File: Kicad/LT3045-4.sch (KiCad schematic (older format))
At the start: 22 parts, among them J1 Conn_Coaxial_Power, J2 Conn_Coaxial_Power, U1 LT3042, U2 LT3042, U3 LT3042, U4 LT3042

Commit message: 1st design
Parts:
- C3, C7, C8, C9: symbol Device:C_SPLIT -> LT3045-4-rescue:C_SPLIT-Device-LNA-rescue
- U1, U2, U3, U4: symbol Regulator_Linear:LT3042 -> LT3045-4-rescue:LT3042-Regulator_Linear-LNA-rescue
- gave numbers to parts that had none: 1
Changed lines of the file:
@@
 $EndComp
 $Comp
-L Regulator_Linear:LT3042 U1
+L LT3045-4-rescue:LT3042-Regulator_Linear-LNA-rescue U1
 U 1 1 5F2966C9
 P 5000 1150
@@
 	2700 900  2950 900
 $Comp
-L Device:C_SPLIT C3
+L LT3045-4-rescue:C_SPLIT-Device-LNA-rescue C3
 U 1 1 5F3E0394
 P 5850 1350
@@
 $EndComp
 $Comp
-L Regulator_Linear:LT3042 U2
+L LT3045-4-rescue:LT3042-Regulator_Linear-LNA-rescue U2
 U 1 1 5F43CBE8
 P 5000 3000
@@
 50mOhm\nTrace
 $Comp
-L Device:C_SPLIT C7
+L LT3045-4-rescue:C_SPLIT-Device-LNA-rescue C7
 U 1 1 5F43CC30
 P 5850 3200
@@
 $EndComp
 $Comp
-L Regulator_Linear:LT3042 U3
+L LT3045-4-rescue:LT3042-Regulator_Linear-LNA-rescue U3
 U 1 1 5F442849
 P 5000 4750
@@
 50mOhm\nTrace
 $Comp
-L Device:C_SPLIT C8
+L LT3045-4-rescue:C_SPLIT-Device-LNA-rescue C8
 U 1 1 5F442891
 P 5850 4950
@@
 $EndComp
 $Comp
-L Regulator_Linear:LT3042 U4
+L LT3045-4-rescue:LT3042-Regulator_Linear-LNA-rescue U4
 U 1 1 5F44B383
 P 5000 6600
@@
 50mOhm\nTrace
 $Comp
-L Device:C_SPLIT C9
+L LT3045-4-rescue:C_SPLIT-Device-LNA-rescue C9
 U 1 1 5F44B3CB
 P 5850 6800
@@
 VIN
 $Comp
-L Device:R_US R?
+L Device:R_US R1
 U 1 1 5FCF17CA
 P 4250 1250
-F 0 "R?" H 4318 1296 50  0000 L CNN
+F 0 "R1" H 4318 1296 50  0000 L CNN
 F 1 "200k" H 4318 1205 50  0000 L CNN
 F 2 "Resistor_SMD:R_0603_1608Metric" V 4290 1240 50  0001 C CNN

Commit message: VIAS
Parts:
- added C11, C4, C5, C6: 4.7µF 35V, Capacitor_SMD:C_0805_2012Metric, symbol Device:C
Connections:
- net GND_SET1: now also C11.2, C4.2, C5.2, C6.2
- net at C2.1, R3.1, U1.7 (SET)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: now also C11.1, C4.1, C5.1, C6.1
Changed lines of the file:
@@
 	2300 1500 1700 1500
-Wire Wire Line
-	4200 1750 4000 1750
-Wire Wire Line
-	4000 1750 4000 3600
 Wire Wire Line
 	4000 3600 4750 3600
@@
 	4750 5250 4750 5350
 Wire Wire Line
-	4750 5350 4000 5350
-Wire Wire Line
-	4000 5350 4000 3600
-Connection ~ 4000 3600
-Wire Wire Line
 	4750 7100 4750 7200
-Wire Wire Line
-	4750 7200 4000 7200
-Wire Wire Line
-	4000 7200 4000 5350
-Connection ~ 4000 5350
 Connection ~ 4200 2200
 Wire Wire Line
@@
 Wire Wire Line
 	5750 3450 5750 4150
+$Comp
+L Device:C C4
+U 1 1 5FD57A1A
+P 3950 2000
+F 0 "C4" H 4065 2046 50  0000 L CNN
+F 1 "4.7µF 35V" H 4065 1955 50  0000 L CNN
+F 2 "Capacitor_SMD:C_0805_2012Metric" H 3988 1850 50  0001 C CNN
+F 3 "~" H 3950 2000 50  0001 C CNN
+	1    3950 2000
+	1    0    0    -1
+$EndComp
+$Comp
+L Device:C C5
+U 1 1 5FD5D837
+P 4000 3850
+F 0 "C5" H 4115 3896 50  0000 L CNN
+F 1 "4.7µF 35V" H 4115 3805 50  0000 L CNN
+F 2 "Capacitor_SMD:C_0805_2012Metric" H 4038 3700 50  0001 C CNN
+F 3 "~" H 4000 3850 50  0001 C CNN
+	1    4000 3850
+	1    0    0    -1
+$EndComp
+$Comp
+L Device:C C6
+U 1 1 5FD6373A
+P 4000 5600
+F 0 "C6" H 4115 5646 50  0000 L CNN
+F 1 "4.7µF 35V" H 4115 5555 50  0000 L CNN
+F 2 "Capacitor_SMD:C_0805_2012Metric" H 4038 5450 50  0001 C CNN
+F 3 "~" H 4000 5600 50  0001 C CNN
+	1    4000 5600
+	1    0    0    -1
+$EndComp
+$Comp
+L Device:C C11
+U 1 1 5FD69ACD
+P 4000 7450
+F 0 "C11" H 4115 7496 50  0000 L CNN
+F 1 "4.7µF 35V" H 4115 7405 50  0000 L CNN
+F 2 "Capacitor_SMD:C_0805_2012Metric" H 4038 7300 50  0001 C CNN
+F 3 "~" H 4000 7450 50  0001 C CNN
+	1    4000 7450
+	1    0    0    -1
+$EndComp
+Wire Wire Line
+	3950 1750 3950 1850
+Connection ~ 3950 1750
+Wire Wire Line
+	3950 1750 4200 1750
+Wire Wire Line
+	4000 3700 4000 3600
+Wire Wire Line
+	3750 1750 3750 3600
+Wire Wire Line
+	3750 3600 4000 3600
+Wire Wire Line
+	3750 1750 3950 1750
+Connection ~ 4000 3600
+Wire Wire Line
+	3750 3600 3750 5350
+Wire Wire Line
+	3750 5350 4000 5350
+Connection ~ 3750 3600
+Wire Wire Line
+	4000 5450 4000 5350
+Connection ~ 4000 5350
+Wire Wire Line
+	4000 5350 4750 5350
+Wire Wire Line
+	4200 5950 4000 5950
+Wire Wire Line
+	4000 5950 4000 5750
+Wire Wire Line
+	4200 4150 4000 4150
+Wire Wire Line
+	4000 4150 4000 4000
+Wire Wire Line
+	4200 2200 3950 2200
+Wire Wire Line
+	3950 2200 3950 2150
+Wire Wire Line
+	3750 5350 3750 7200
+Connection ~ 3750 5350
+Wire Wire Line
+	3750 7200 4000 7200
+Wire Wire Line
+	4000 7300 4000 7200
+Connection ~ 4000 7200
+Wire Wire Line
+	4000 7200 4750 7200
+Wire Wire Line
+	4000 7600 4000 7750
+Wire Wire Line
+	4000 7750 4200 7750
+Connection ~ 4200 7750
 $EndSCHEMATC

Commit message: Lost revision :(
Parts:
- added C12: 22µF 35V, Capacitor_Tantalum_SMD:CP_EIA-7343-30_AVX-N, symbol Device:CP1
- added C13: 4.7µF 35V, Capacitor_SMD:C_0805_2012Metric, symbol Device:C
- added F1: 4A, Fuse:Fuse_Bourns_MF-SM_9.5x6.71mm, symbol Device:Polyfuse_Small
- added L1: DLW5BTH101TQ2L, Transformer_SMD:CMC_DLW5BTH, symbol Device:Common_Mode_Choke
- added MH1, MH2, MH3, MH4: MountingHole_Pad, MountingHole:MountingHole_3.2mm_M3, symbol Mechanical:MountingHole_Pad
- added R2: 16.5k, Resistor_SMD:R_0603_1608Metric, symbol Device:R_US
- added Rcdc1: Rcdc, Resistor_SMD:R_0603_1608Metric, symbol Device:R_US
- RIlim1: renamed from R14; value 0 -> 287
- RIlim2: renamed from R4; value 0 -> 287
- RIlim3: renamed from R15; value 0 -> 287
- RIlim4: renamed from R16; value 0 -> 287
- renumbered L1 to L2, R3 to Rset1
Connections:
- net GND: now also C12.2, C13.2, L1.3, MH1.1, MH2.1, MH3.1, MH4.1, Rcdc1.2; no longer J1.2 (Ext), RIlim1.2, RIlim2.2, RIlim3.2, RIlim4.2
- net at C11.1, C2.1, C4.1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: now also R2.1
- net at C1.1, C10.1, L2.2: now also C12.1, C13.1, L1.2; no longer J1.1 (In)
- new net: F1.2, J1.1 (In)
- new net: J1.2 (Ext), L1.4
- new net: F1.1, L1.1
- new net ILim: R2.2, RIlim1.2, RIlim2.2, RIlim3.2, RIlim4.2, Rcdc1.1
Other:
- note added: "20/50mOhm\nTrace"
- note added: "Res = width length PCB weigth Temp \n50mOhm = 0.1mm 27.6mm 2oz/ft² -40C\n = 0.2mm 27.6mm 1oz/ft² -40C\n = 0.4mm 27.6mm 0.5oz/ft² -40C\n20mOhm = 0.25mm 27.6mm 2oz/ft² -40C\n = 0.5mm 27.6mm 1oz/ft² -40C\n = 1.0mm 27.6mm 0.5oz/ft² -40C"
- note removed: "50mOhm\nTrace"
- note removed: "Res = width length PCB weigth Temp \n50mOhm = 0.1mm 27.6mm 2oz/ft² -40C\n = 0.2mm 27.6mm 1oz/ft² -40C\n"
- moved on the sheet: C1, C10, C11, C2, C3, C4, C5, C6, C7, C8, C9, J1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

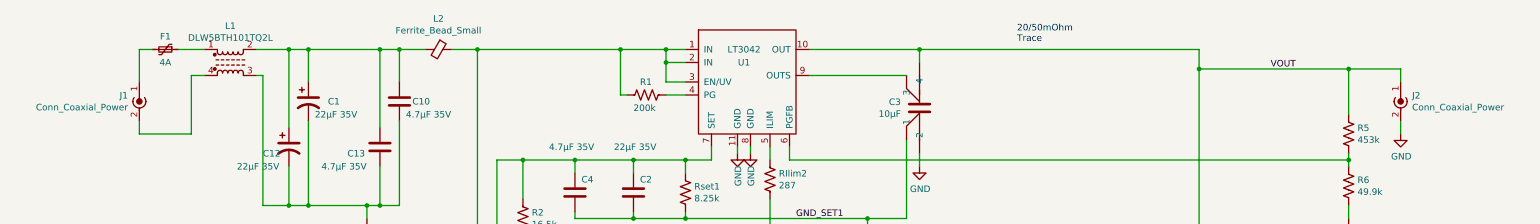
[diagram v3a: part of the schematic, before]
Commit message: line width mistake corrected on silk screen
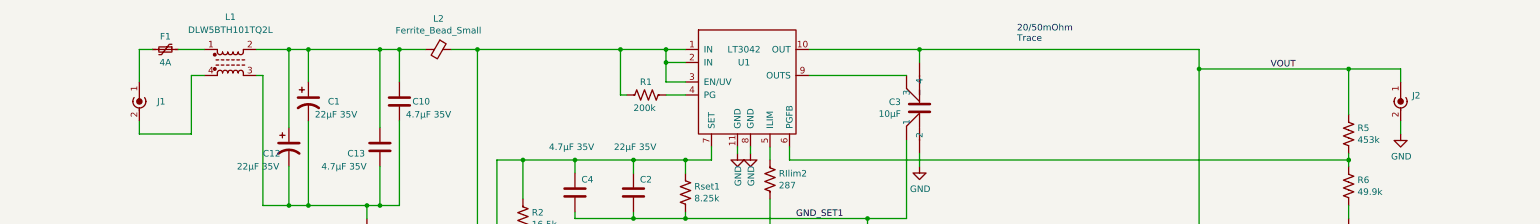
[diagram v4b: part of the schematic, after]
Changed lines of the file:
@@
 encoding utf-8
 Sheet 1 1
-Title ""
-Date ""
-Rev ""
+Title "LT3045/LT3042-4"
+Date "2020-12-14"
+Rev "0.5"
 Comp ""
 Comment1 ""
@@
 P 10350 1150
 F 0 "J2" H 10438 1146 50  0000 L CNN
-F 1 "Conn_Coaxial_Power" H 10438 1055 50  0000 L CNN
+F 1 "Conn_Coaxial_Power" H 10438 1055 50  0001 L CNN
 F 2 "Connector_Coaxial:SMA_Amphenol_132289_EdgeMount" H 10350 1100 50  0001 C CNN
 F 3 "~" H 10350 1100 50  0001 C CNN
@@
 U 1 1 5F2AD177
 P 650 1150
-F 0 "J1" H 738 1146 50  0000 L CNN
-F 1 "Conn_Coaxial_Power" H 738 1055 50  0000 L CNN
+F 0 "J1" H 450 1100 50  0000 L CNN
+F 1 "Conn_Coaxial_Power" H 50  650 50  0001 L CNN
 F 2 "Connector_Coaxial:SMA_Amphenol_132289_EdgeMount" H 650 1100 50  0001 C CNN
 F 3 "~" H 650 1100 50  0001 C CNN
@@
 U 1 1 6094D9EE
 P 1350 900
-F 0 "L1" H 1350 1181 50  0000 C CNN
-F 1 "DLW5BTH101TQ2L" H 1350 1090 50  0000 C CNN
+F 0 "L1" H 1350 1250 50  0000 C CNN
+F 1 "DLW5BTH101TQ2L" H 1350 1150 50  0000 C CNN
 F 2 "Transformer_SMD:CMC_DLW5BTH" H 1350 900 50  0001 C CNN
 F 3 "~" H 1350 900 50  0001 C CNN
